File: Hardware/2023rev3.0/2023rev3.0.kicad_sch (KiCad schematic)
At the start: 223 parts, among them J1 Conn_01x03, J2 Conn_01x09, J3 Conn_01x09, J4 Conn_01x04, Q1 Q_NMOS_DGS, Q10 Q_NMOS_DGS, Q11 Q_NMOS_DGS, Q12 Q_PMOS_DGS, Q2 Q_PMOS_DGS, Q3 Q_PMOS_DGS, Q4 Q_PMOS_DGS, Q5 Q_PMOS_DGS, Q6 Q_PMOS_DGS, Q7 Q_PMOS_DGS, Q8 Q_PMOS_DGS, Q9 Q_PMOS_DGS, SW1 SW_SPDT, T1 Transformer_1P_1S, T2 Transformer_1P_1S, T3 Transformer_1P_1S, T4 Transformer_1P_1S, T5 Transformer_1P_1S, T6 Transformer_1P_1S, T7 Transformer_1P_1S, T8 Transformer_1P_1S, U1 Teensy4.1_DEV-16771, U2 Opamp_Dual, U3 Opamp_Dual, U4 Opamp_Dual, U5 Opamp_Dual, U6 INA195, U7 OKI, U8 TSR_1-2450

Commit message: Updated to where rev 2 is
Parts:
- removed BZ1: Buzzer, MRDT_Devices:BUZZER_SMI_1324_TW_5V_2_R, symbol Device:Buzzer
- removed C1: 22uF, Capacitor_THT:CP_Radial_D5.0mm_P2.50mm, symbol Device:C_Polarized_US
- removed C2: 1uF, Capacitor_THT:CP_Radial_D5.0mm_P2.50mm, symbol Device:C_Polarized_US
- removed C3: 10uF, Capacitor_THT:CP_Radial_D5.0mm_P2.50mm, symbol Device:C_Polarized_US
- removed unit 1 of Conn1
- removed D1: ERR, LED_SMD:LED_0603_1608Metric_Pad1.05x0.95mm_HandSolder, symbol Device:LED
- removed D10, D11, D12, D5, D6, D7, D8, D9: D_Schottky, Diode_SMD:D_0603_1608Metric_Pad1.05x0.95mm_HandSolder, symbol Device:D_Schottky
- removed D13, D14, D15, D16, D17, D18, D19, D20: D_Zener, Diode_SMD:D_0603_1608Metric_Pad1.05x0.95mm_HandSolder, symbol Device:D_Zener
- removed D2: PACK_OUT, LED_SMD:LED_0603_1608Metric_Pad1.05x0.95mm_HandSolder, symbol Device:LED
- removed D21, D22, D23, D24, D25, D26, D27, D28: D, symbol Device:D
- removed D3: 5V, LED_SMD:LED_0603_1608Metric_Pad1.05x0.95mm_HandSolder, symbol Device:LED
- removed D4: 3V3, LED_SMD:LED_0603_1608Metric_Pad1.05x0.95mm_HandSolder, symbol Device:LED
- removed F1: Polyfuse, Fuse:Fuse_2920_7451Metric_Pad2.10x5.45mm_HandSolder, symbol Device:Polyfuse
- removed H1, H2, H3, H4, H5, H6: MountingHole, MRDT_Drill_Holes:4_40_Hole, symbol Mechanical:MountingHole
- removed J1: Conn_01x03, MRDT_Connectors:MOLEX_SL_03_Vertical, symbol Connector_Generic:Conn_01x03
- removed J2, J3: Conn_01x09, MRDT_Connectors:MOLEX_SL_09_Vertical, symbol Connector_Generic:Conn_01x09
- removed J4: Conn_01x04, MRDT_Connectors:MOLEX_SL_04_Vertical, symbol Connector_Generic:Conn_01x04
- removed Q1: Q_NMOS_DGS, Package_TO_SOT_SMD:SOT-23_Handsoldering, symbol Device:Q_NMOS_DGS
- removed Q10, Q11: Q_NMOS_DGS, symbol Device:Q_NMOS_DGS
- removed Q12, Q2, Q3, Q4, Q5, Q6, Q7, Q8, Q9: Q_PMOS_DGS, symbol Device:Q_PMOS_DGS
- removed R1: 100K, Resistor_SMD:R_0603_1608Metric_Pad0.98x0.95mm_HandSolder, symbol Device:R
- removed R10, R11, R12, R13, R14, R15, R16, R17, R18, R19, R20, R21, R22, R23, R24, R9: 31.5k, Resistor_SMD:R_0603_1608Metric_Pad0.98x0.95mm_HandSolder, symbol Device:R
- removed R2: 4.7k, Resistor_SMD:R_0603_1608Metric_Pad0.98x0.95mm_HandSolder, symbol Device:R
- removed R25, R26, R27, R28, R29, R30, R31, R32, R33, R34, R35, R36, R37, R38, R39, R40: 40k, Resistor_SMD:R_0603_1608Metric_Pad0.98x0.95mm_HandSolder, symbol Device:R
- removed R3: 820, Resistor_SMD:R_0603_1608Metric_Pad0.98x0.95mm_HandSolder, symbol Device:R
- removed R4, R43: 10k, Resistor_SMD:R_0603_1608Metric_Pad0.98x0.95mm_HandSolder, symbol Device:R
- removed R41: 4k, Resistor_SMD:R_0603_1608Metric_Pad0.98x0.95mm_HandSolder, symbol Device:R
- removed R44: 6.8K, symbol Device:R
- removed R45: 3.3K, symbol Device:R
- removed R5, R8: 100, Resistor_SMD:R_0603_1608Metric_Pad0.98x0.95mm_HandSolder, symbol Device:R
- removed R6: 3k, Resistor_SMD:R_0603_1608Metric_Pad0.98x0.95mm_HandSolder, symbol Device:R
- removed R7: 300, Resistor_SMD:R_0603_1608Metric_Pad0.98x0.95mm_HandSolder, symbol Device:R
- removed SW1: SW_SPDT, MRDT_Connectors:MOLEX_SL_03_Horizontal, symbol Switch:SW_SPDT
- removed T1, T2, T3, T4, T5, T6, T7, T8: Transformer_1P_1S, symbol Device:Transformer_1P_1S
- removed U1: Teensy4.1_DEV-16771, MRDT_Shields:Teensy_4_1, symbol MRDT_Shields:Teensy4.1_DEV-16771
- removed U2, U3, U4, U5: Opamp_Dual, Package_SO:SO-8_3.9x4.9mm_P1.27mm, symbol Device:Opamp_Dual
- removed U7: OKI, symbol MRDT_Devices:OKI
- removed U8: TSR_1-2450, Converter_DCDC:Converter_DCDC_TRACO_TSR-1_THT, symbol Regulator_Switching:TSR_1-2433
- removed V1: BATT_GND_VIA, MRDT_Drill_Holes:BATT_PWR_VIA, symbol MRDT_Drill_Holes:BATT_PWR_VIA
- removed V3: BMS_OUT_VIA, MRDT_Drill_Holes:BATT_PWR_VIA, symbol MRDT_Drill_Holes:BATT_PWR_VIA
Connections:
- no-connect marks 39 -> 38
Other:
- note removed: "0-8 PWM pins"
- note removed: "Cell Sense"
- note removed: "Current Sense"
- note removed: "E-Stop"
- note removed: "Transformer Balance Circuit"
- moved on the sheet: BZ?, C?, Conn1B, Conn?A, Conn?B, D?, F?, H?, J?, Q?, R42, R?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

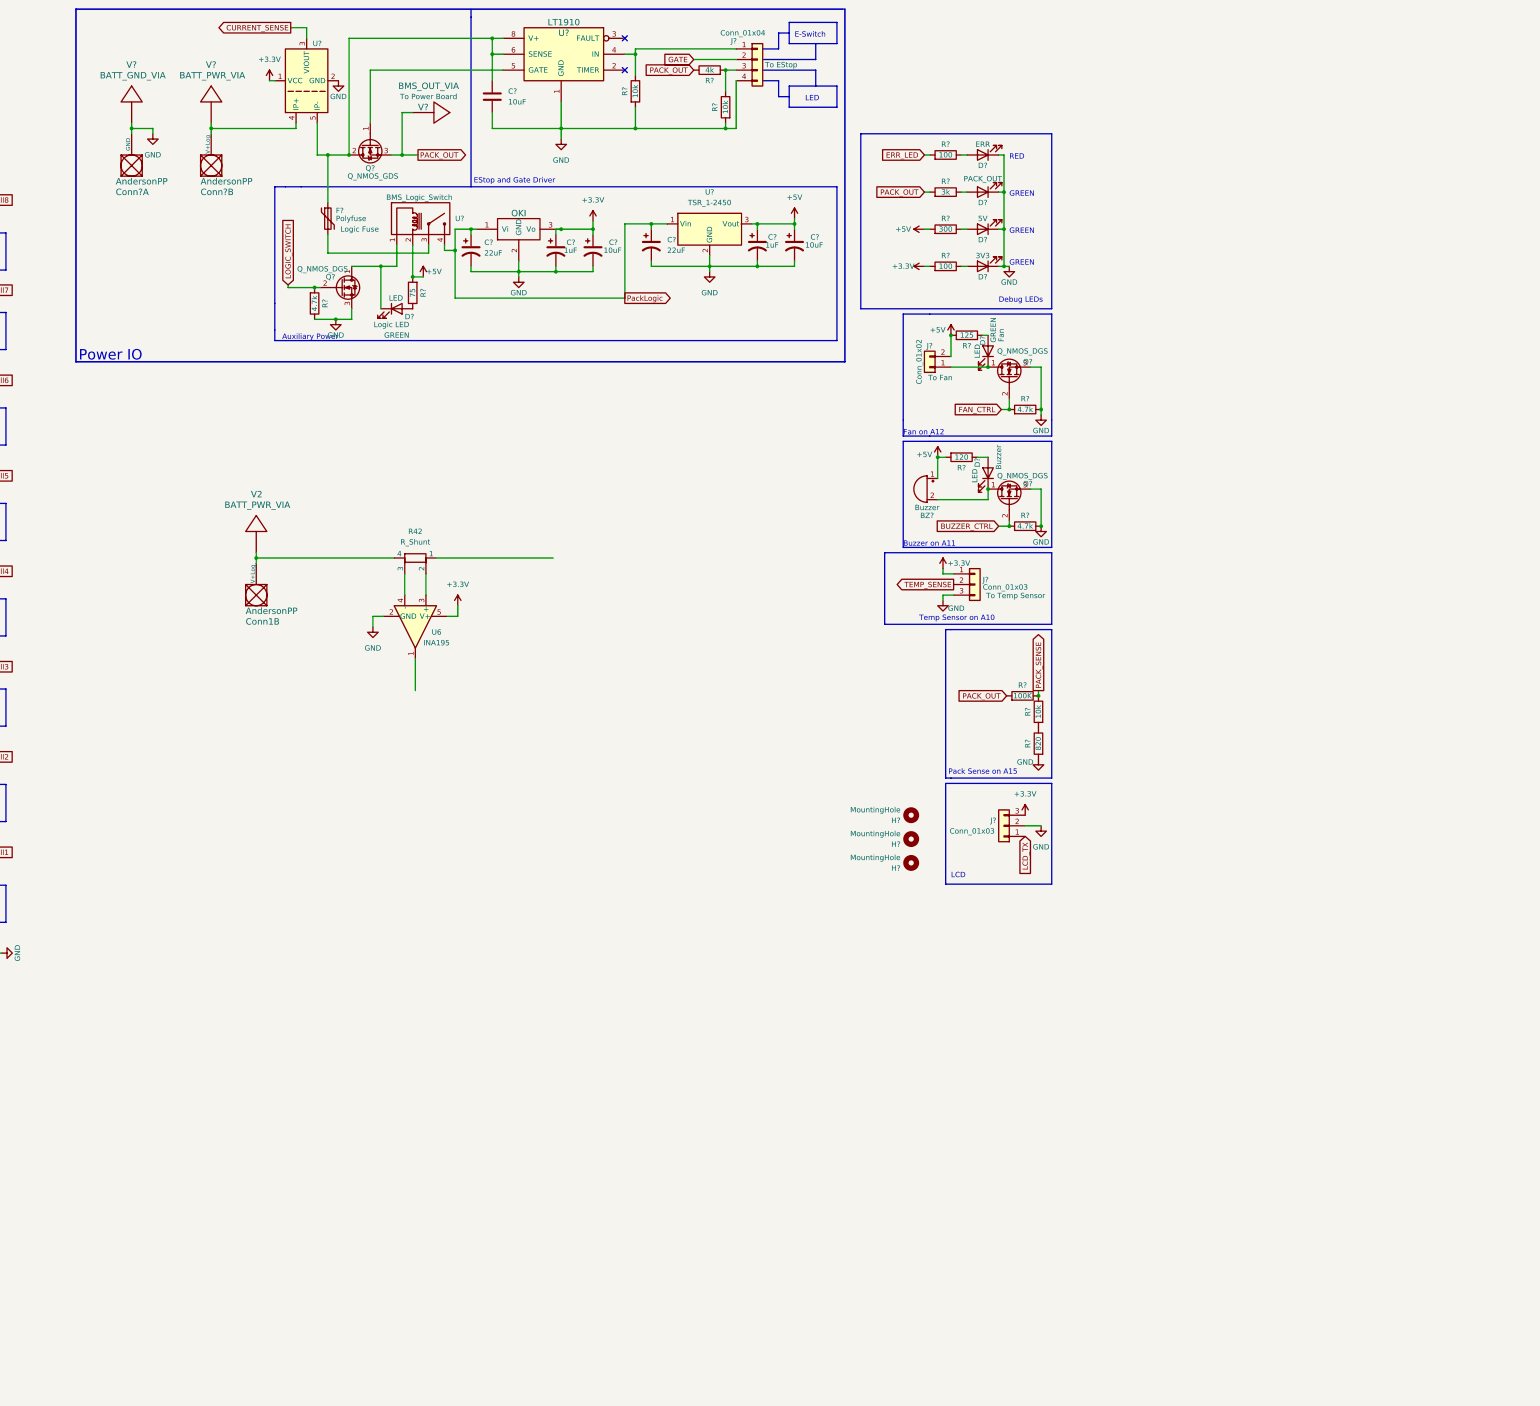
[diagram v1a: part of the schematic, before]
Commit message: Added alternate high side toggling with mosfet circuit
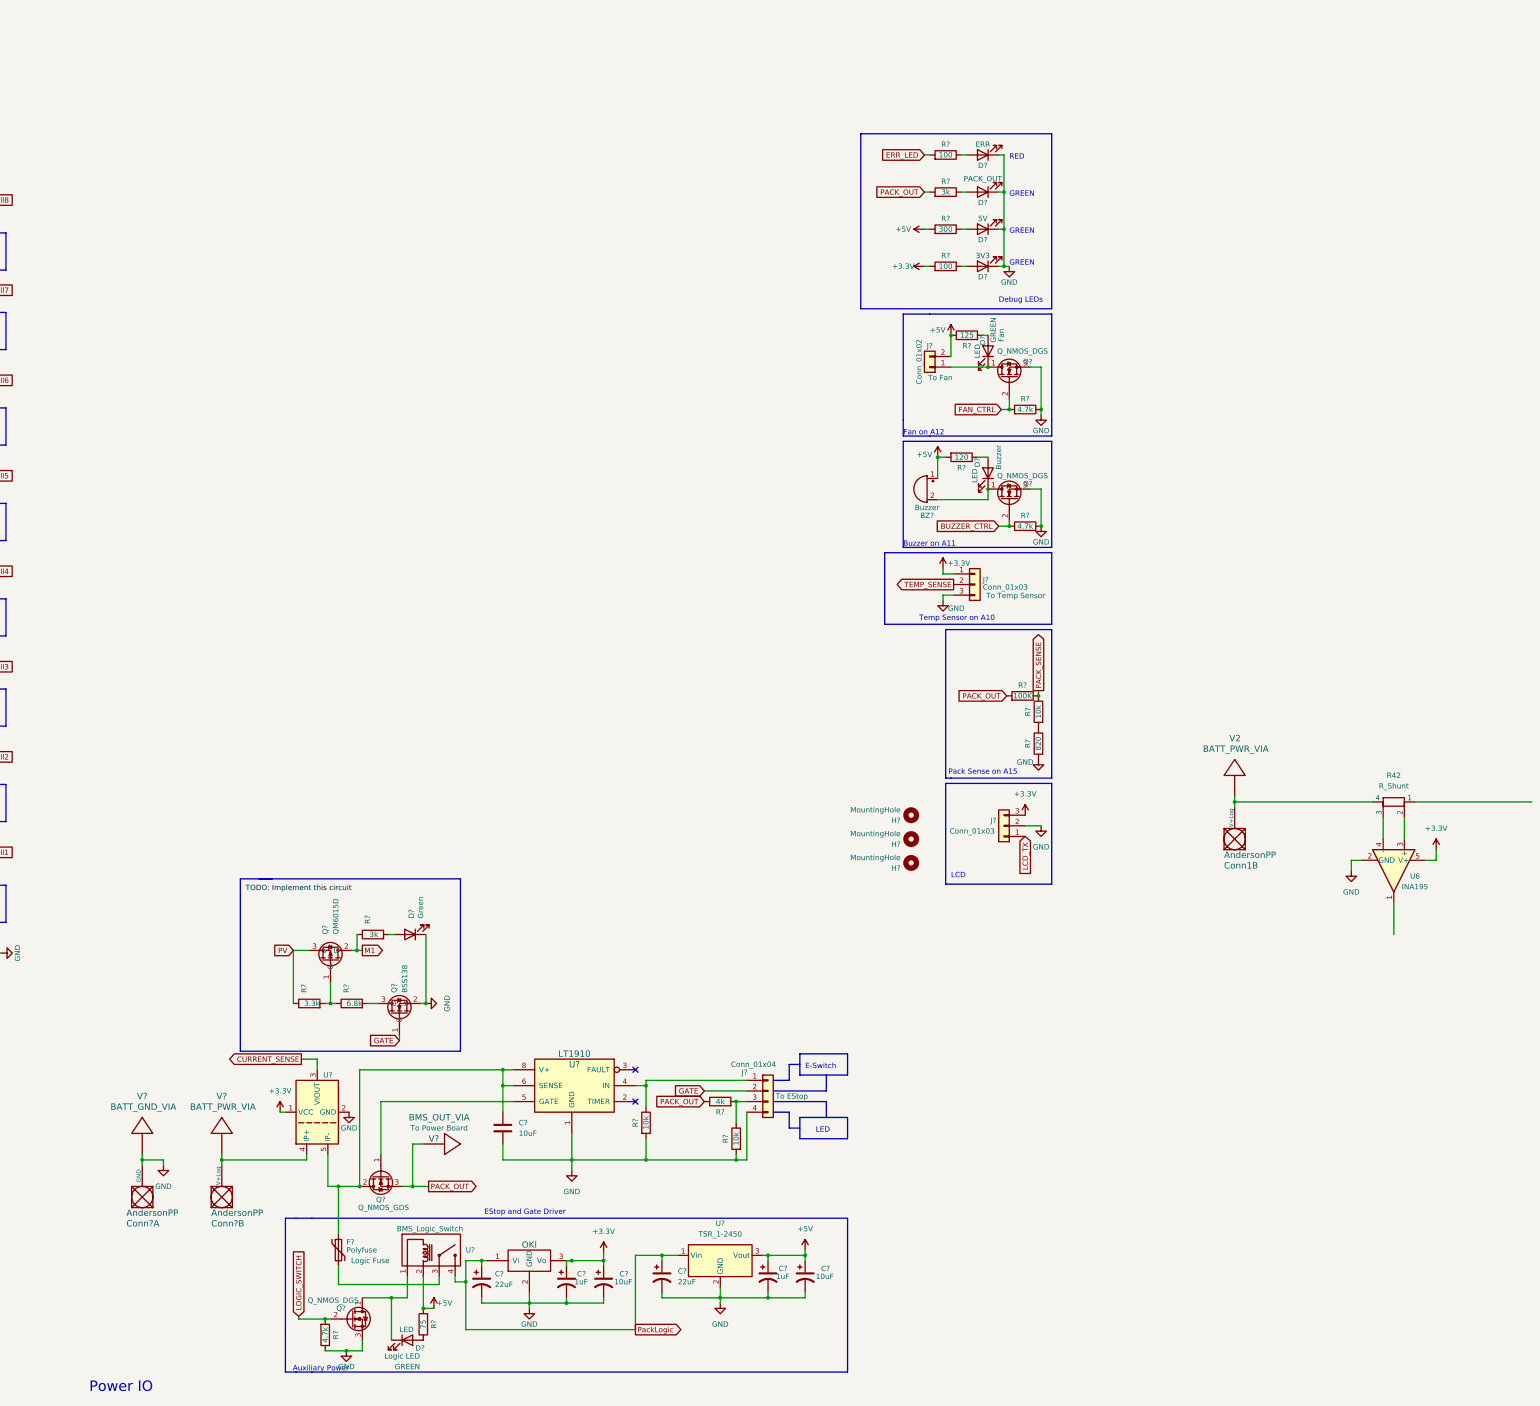
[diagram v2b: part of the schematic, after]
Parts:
- added D?: Green, LED_SMD:LED_0603_1608Metric_Pad1.05x0.95mm_HandSolder, symbol Device:LED
- added Q?: QM6015D, Package_TO_SOT_SMD:TO-252-2, symbol Transistor_FET:QM6015D
- added Q?: BSS138, Package_TO_SOT_SMD:SOT-23, symbol Transistor_FET:BSS138
- added R?: 3.3k, Resistor_SMD:R_0603_1608Metric_Pad0.98x0.95mm_HandSolder, symbol Device:R
- added R?: 3k, Resistor_SMD:R_0603_1608Metric_Pad0.98x0.95mm_HandSolder, symbol Device:R
- added R?: 6.8k, Resistor_SMD:R_0603_1608Metric_Pad0.98x0.95mm_HandSolder, symbol Device:R
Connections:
- net GATE: now also Q?.1 (G)
- net GND: now also D?.1 (K), Q?.2 (S)
- new net: Q?.1 (G), R?.1, R?.2
- new net: D?.2 (A), R?.2
- new net: Q?.3 (D), R?.2
- new net M1: Q?.2 (D), R?.1
- new net PV: Q?.3 (S), R?.1
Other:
- moved on the sheet: C?, Conn1B, Conn?A, Conn?B, D?, F?, J?, Q?, R42, R?, U6, U?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
